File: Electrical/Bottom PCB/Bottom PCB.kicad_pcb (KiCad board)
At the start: 2 copper layers, 100 x 80 mm, 61 parts, among them J101 Steper1, J102 Steper2, J104 Servo1, J105 Servo2, J106 Servo3, J107 Servo4, J201 PROGRAMMING, J202 MainIO, Q201 BC847, Q202 BC847, SW101 FL, SW102 FR, U101 ULN2003A, U103 QRE1113, U106 QRE1113, U107 MCP23017_SO, U108 QRE1113, U109 QRE1113, U201 ESP32-WROVER

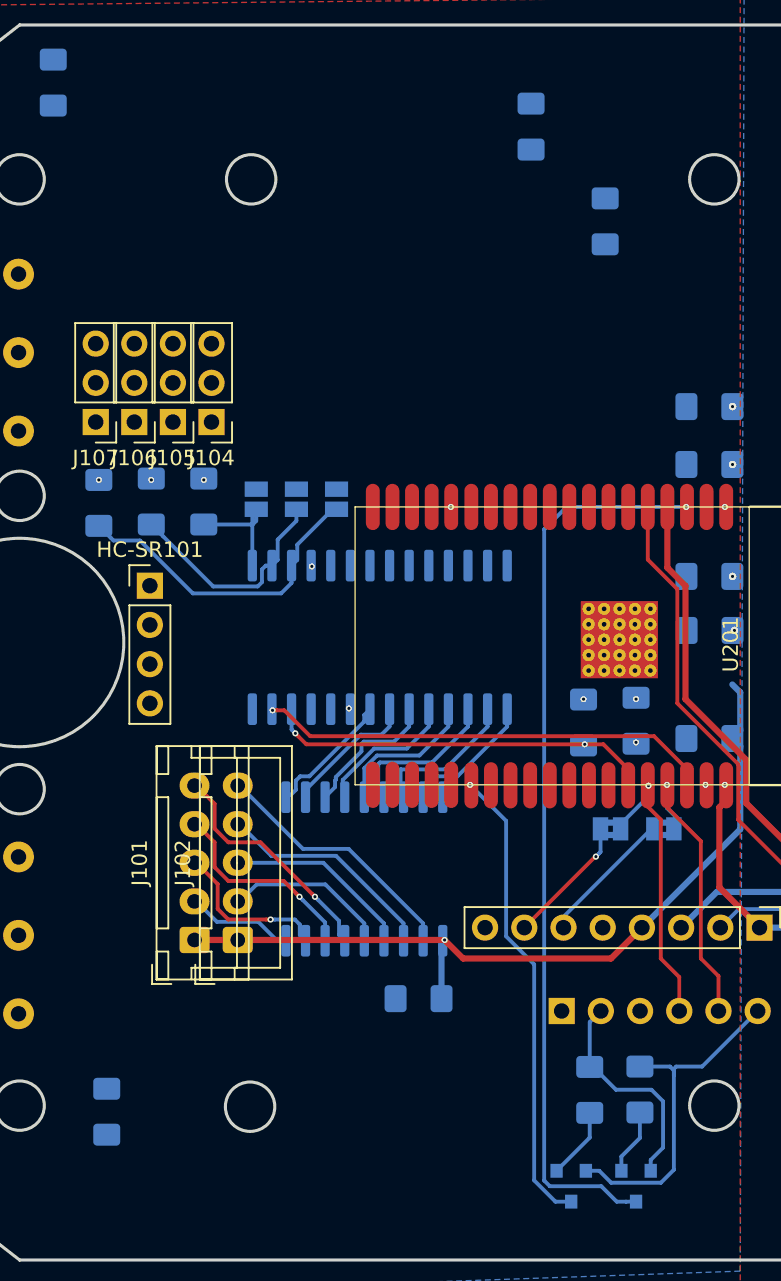
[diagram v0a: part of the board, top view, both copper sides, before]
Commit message: moved some parts to 5V supply
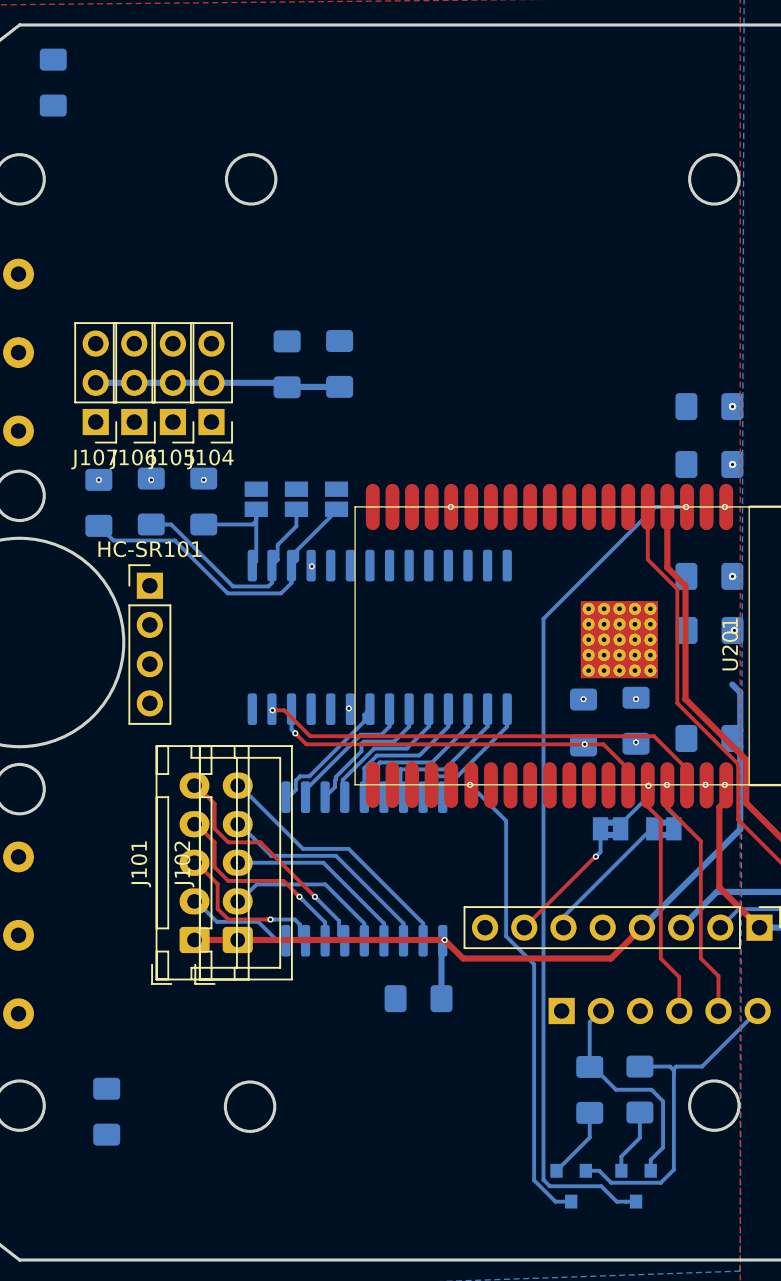
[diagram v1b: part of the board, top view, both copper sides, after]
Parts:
- moved C103 22.1 mm to (136.4, 71.5)
- moved C102 19.5 mm to (139.8, 71.5)
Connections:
- J104 pad 2: Net-(J104-Pad2) -> +5V
- J105 pad 2: Net-(J104-Pad2) -> +5V
- J106 pad 2: Net-(J104-Pad2) -> +5V
- J107 pad 2: Net-(J104-Pad2) -> +5V
- R104 pad 2: +5V -> +3V3
- R106 pad 2: +5V -> +3V3
- R108 pad 2: +5V -> +3V3
- R113 pad 2: +5V -> +3V3
- SW101 pad 1: +5V -> +3V3
- SW102 pad 1: +5V -> +3V3
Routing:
- net +5V: track 53.1 -> 69.0 mm
- net EN: track 58.5 -> 55.2 mm

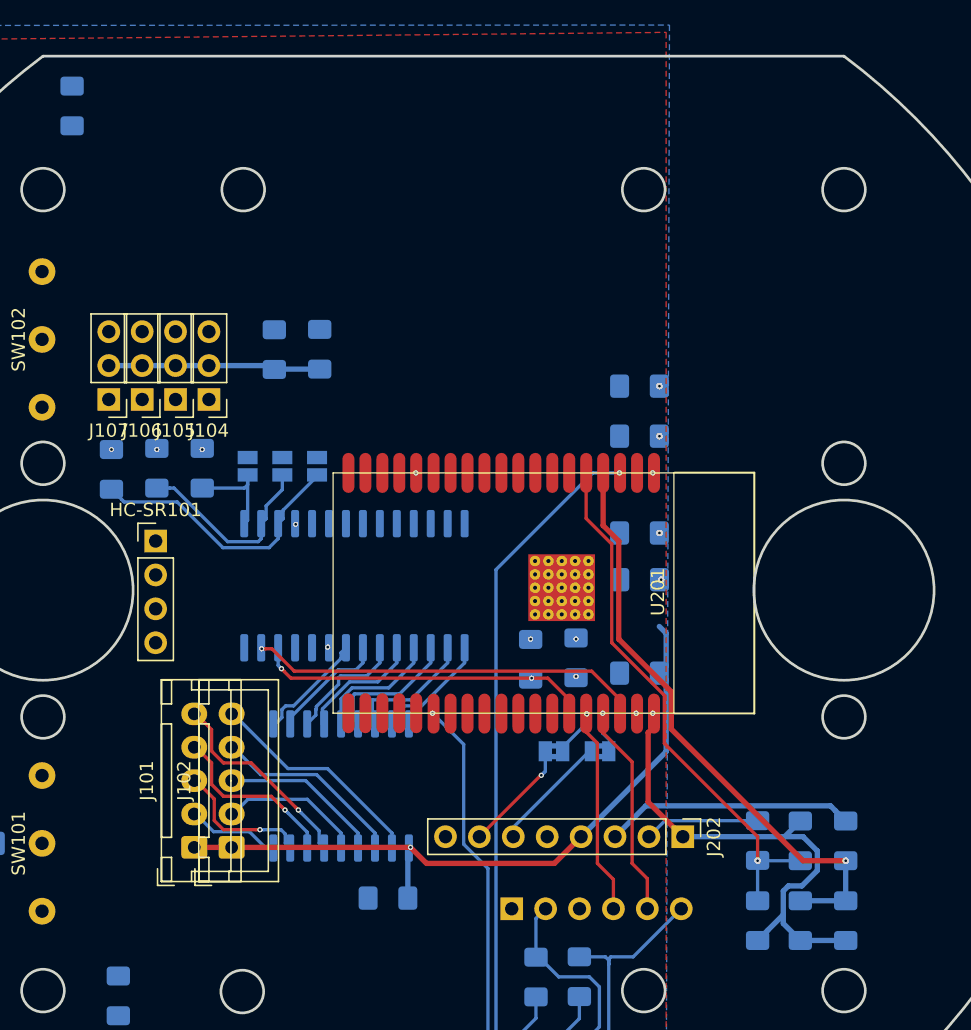
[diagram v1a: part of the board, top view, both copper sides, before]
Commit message: removed the servos at the moment
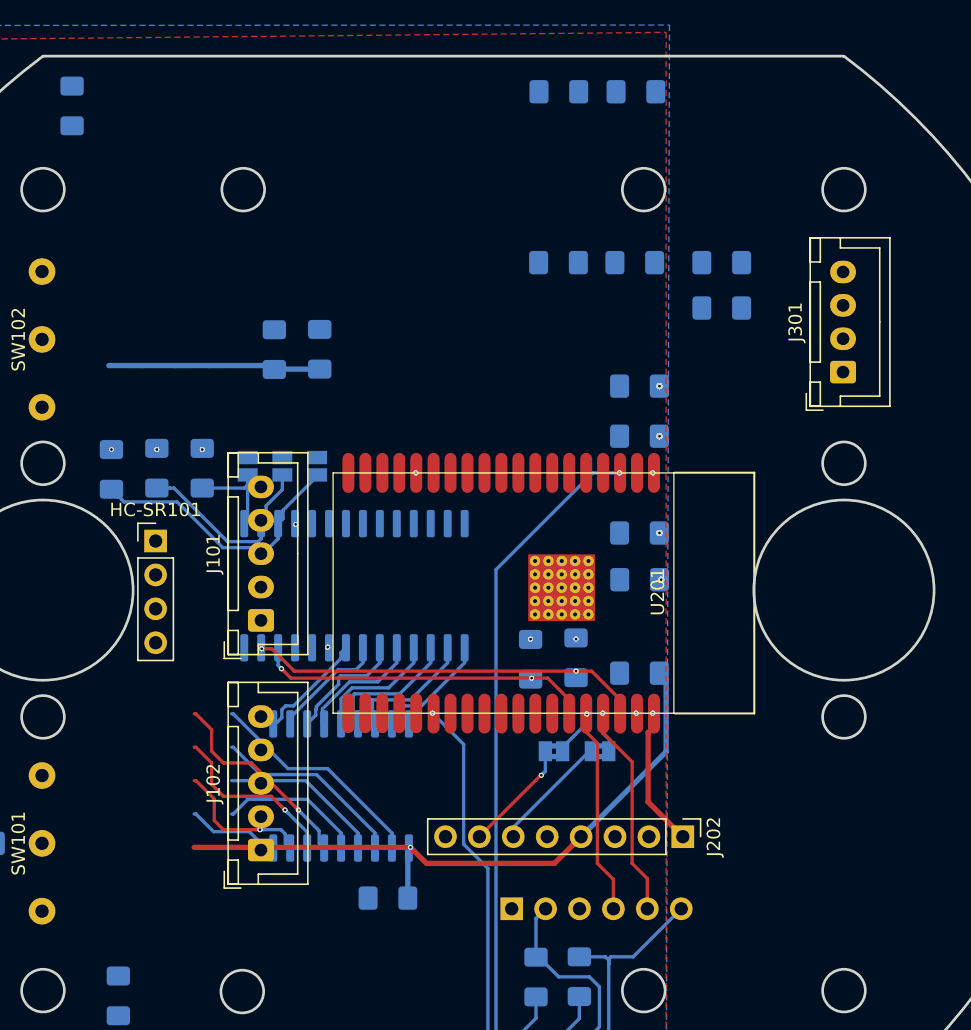
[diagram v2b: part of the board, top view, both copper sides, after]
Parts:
- removed J104: Servo1, Connector_PinHeader_2.54mm:PinHeader_1x03_P2.54mm_Vertical
- removed J105: Servo2, Connector_PinHeader_2.54mm:PinHeader_1x03_P2.54mm_Vertical
- removed J106: Servo3, Connector_PinHeader_2.54mm:PinHeader_1x03_P2.54mm_Vertical
- removed J107: Servo4, Connector_PinHeader_2.54mm:PinHeader_1x03_P2.54mm_Vertical
- added J301: Battery, Connector_JST:JST_XH_B4B-XH-A_1x04_P2.50mm_Vertical, F.Cu at (179.0, 73.2)
- moved C301 64.7 mm to (157.7, 52.2), turned to 0 degrees
- moved R304 62.8 mm to (163.5, 52.2), turned to 0 degrees
- moved R302 53.8 mm to (157.7, 65.0), turned to 180 degrees
- moved C302 45.1 mm to (163.4, 65.0), turned to 180 degrees
- moved R303 43.4 mm to (169.9, 65.0), turned to 0 degrees
- moved R301 41.0 mm to (169.9, 68.4), turned to 0 degrees
- moved J101 17.7 mm to (135.4, 91.8)
- moved J102 2.21 mm to (135.4, 109.0)
- renumbered C107 to C103, C103 to C104, C104 to C105, C109 to C106, C110 to C107, C111 to C108, R109 to R105, R110 to R106, R111 to R107, R105 to R108, R106 to R109, R107 to R110, R108 to R111, U103 to U102, U107 to U103, U106 to U104, U108 to U105, U109 to U106
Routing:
- net BatV: track 44.9 -> 0.00 mm, vias 1 -> 0
- net half_BatV: track 40.6 -> 0.00 mm, vias 1 -> 0
- net GND: track 37.7 -> 10.5 mm
- net +BATT: track 18.7 -> 0.00 mm
- net +3V8: track 8.64 -> 0.00 mm
- net +5V: track 69.0 -> 65.1 mm

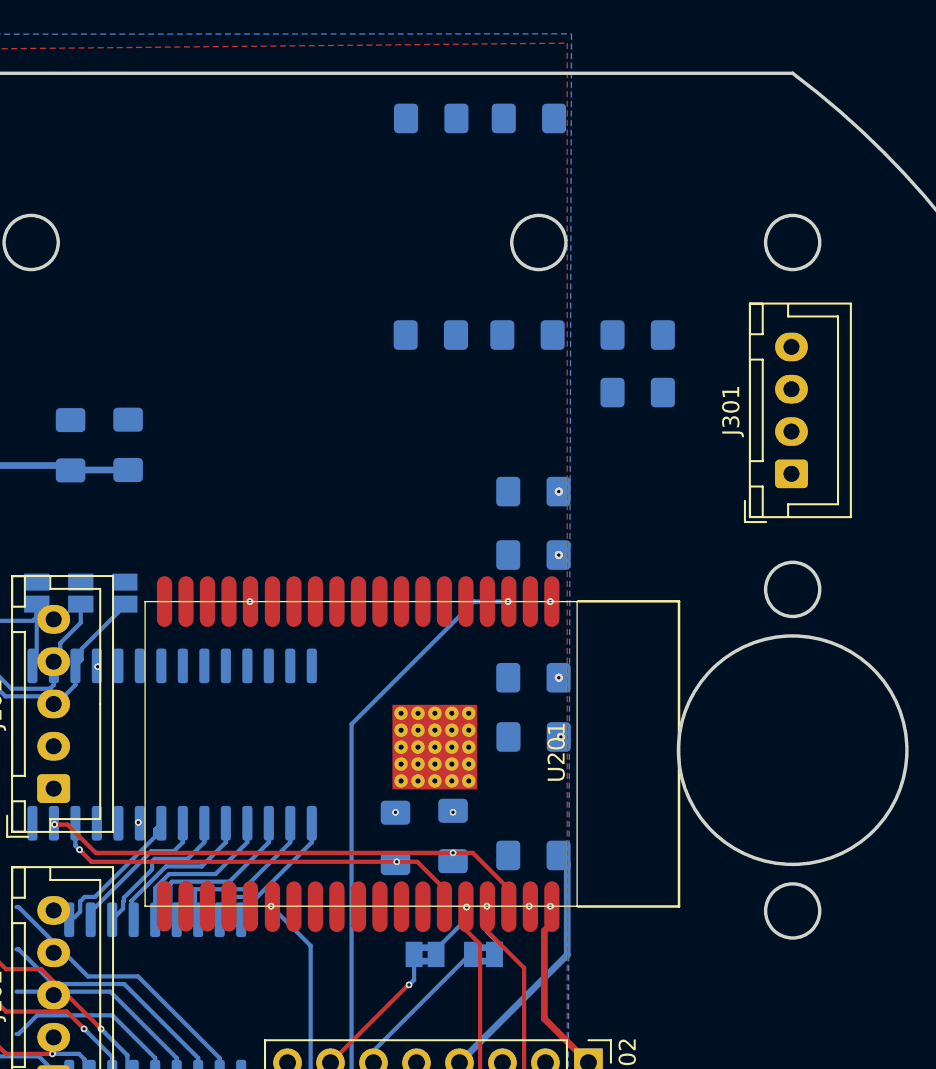
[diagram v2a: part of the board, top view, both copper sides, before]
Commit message: Added power switch
Some more modifications
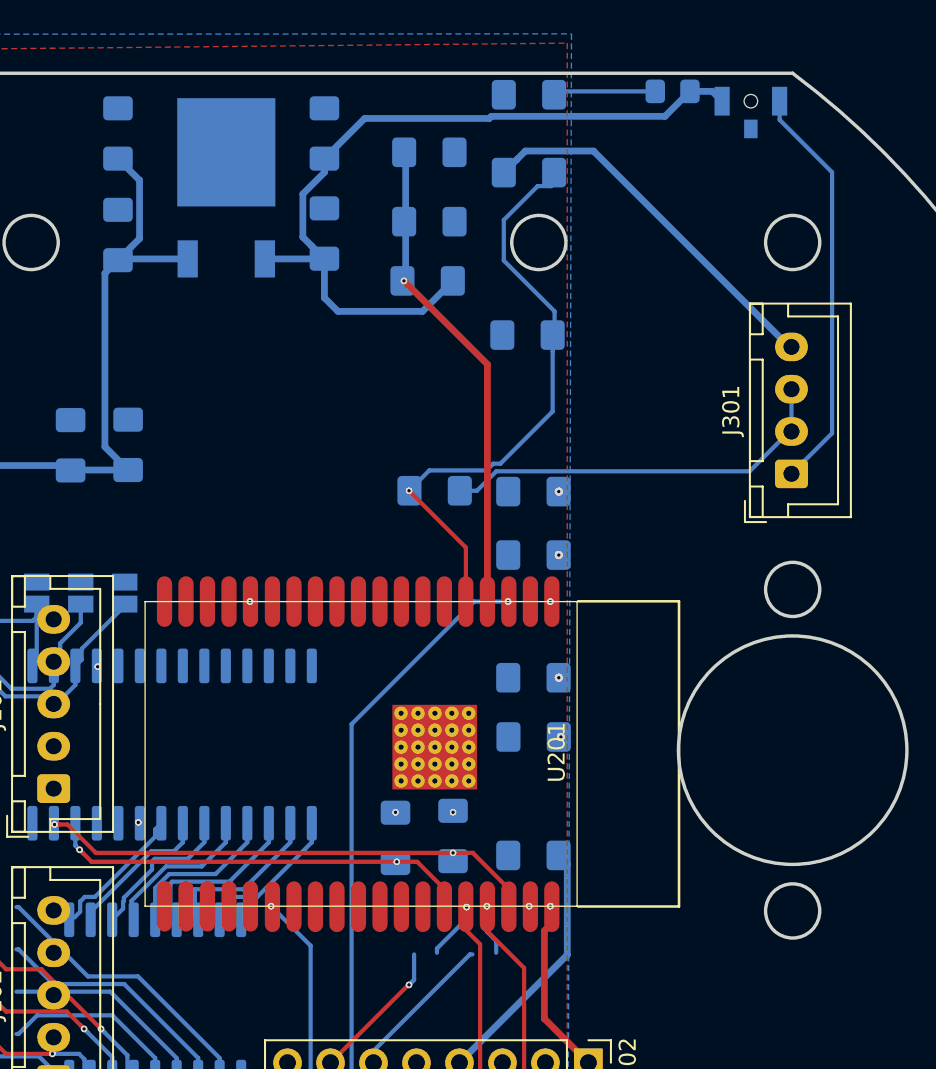
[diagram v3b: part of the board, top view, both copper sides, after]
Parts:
- removed JP201, JP202: Jumper_2_Bridged, Jumper:SolderJumper-2_P1.3mm_Bridged2Bar_Pad1.0x1.5mm
- added C302: 100pF, Capacitor_SMD:C_1206_3216Metric_Pad1.42x1.75mm_HandSolder, B.Cu at (151.4, 59.0)
- added C303: 10uF, Capacitor_SMD:C_1206_3216Metric_Pad1.42x1.75mm_HandSolder, B.Cu at (151.4, 53.1)
- added C304: 10uF, Capacitor_SMD:C_1206_3216Metric_Pad1.42x1.75mm_HandSolder, B.Cu at (139.2, 59.1)
- added C305: 100pF, Capacitor_SMD:C_1206_3216Metric_Pad1.42x1.75mm_HandSolder, B.Cu at (139.2, 53.1)
- added D301: Power, LED_SMD:LED_0805_2012Metric_Pad1.15x1.40mm_HandSolder, B.Cu at (172.0, 50.6)
- added R305: 470, Resistor_SMD:R_1206_3216Metric_Pad1.42x1.75mm_HandSolder, B.Cu at (163.5, 50.8)
- added SW301: SW_SPST, Button_Switch_SMD:SW_SPST_B3U-3100P-B, B.Cu at (176.6, 52.0)
- added U301: MC78M05_TO252, Package_TO_SOT_SMD:TO-252-2, B.Cu at (145.6, 56.3)
- R107: renamed from R105; value 4k7 -> 47k
- R108: renamed from R106; value 4k7 -> 47k
- R109: renamed from R107; value 4k7 -> 47k
- R301, R303: value 22k -> 47k
- moved R303 15.1 mm to (157.9, 74.2)
- moved R301 14.1 mm to (157.5, 61.8)
- moved R302 6.70 mm to (157.6, 58.3)
- moved R304 3.20 mm to (163.5, 55.4)
- moved C301 2.00 mm to (157.6, 54.2)
- renumbered C103 to C101, C101 to C102, C102 to C103, C302 to C306, R108 to R105, R109 to R106, U102 to U101, U101 to U102
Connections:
- J202 pad 2: +3V8 -> (no net)
- J202 pad 3: +BATT -> (no net)
- J202 pad 6: /ESP32-WROVER/TX_sw -> TX
- J202 pad 7: /ESP32-WROVER/RX_sw -> RX
- J301 pad 1: +BATT -> Net-(J301-Pad1)
- J301 pad 2: +3V8 -> half_Bat
- J301 pad 3: +3V8 -> half_Bat
- R303 pad 2: +3V8 -> half_Bat
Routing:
- net +BATT: track 0.00 -> 46.9 mm
- net half_BatV: track 0.00 -> 35.2 mm, vias 0 -> 1
- net BatV: track 0.00 -> 28.6 mm, vias 0 -> 1
- net +5V: track 65.1 -> 89.6 mm
- net Net-(J301-Pad1): track 0.00 -> 24.3 mm
- net half_Bat: track 0.00 -> 23.5 mm
- net GND: track 10.5 -> 32.8 mm
- net TX: track 19.0 -> 27.9 mm
- net /ESP32-WROVER/TX_sw: track 8.91 -> 0.00 mm
- net RX: track 18.9 -> 27.4 mm, vias 1 -> 2
- net /ESP32-WROVER/RX_sw: track 8.47 -> 0.00 mm, vias 1 -> 0
- net Net-(U102-Pad1): track 8.46 -> 0.00 mm
- net Net-(U101-Pad1): track 0.00 -> 8.46 mm
- net Net-(D301-Pad1): track 0.00 -> 6.06 mm

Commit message: added more stuff
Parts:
- added R102: 2k7, Resistor_SMD:R_1206_3216Metric_Pad1.42x1.75mm_HandSolder, B.Cu at (144.5, 106.3)
- added R103: 4k7, Resistor_SMD:R_1206_3216Metric_Pad1.42x1.75mm_HandSolder, B.Cu at (144.5, 103.0)
- moved J201 30.7 mm to (183.0, 102.7), turned to 180 degrees
- moved J101 26.3 mm to (131.8, 65.7), turned to 270 degrees
- moved U102 13.6 mm to (135.8, 91.8), turned to 180 degrees
- moved J202 12.4 mm to (174.9, 98.4), turned to 0 degrees
- moved R201 9.04 mm to (163.9, 102.2)
- moved R202 8.40 mm to (159.2, 102.3)
- moved J102 6.41 mm to (131.8, 103.7), turned to 270 degrees
- moved U103 6.23 mm to (148.6, 88.6), turned to 0 degrees
- renumbered C302 to C301, C303 to C302, C304 to C303, C305 to C304, C301 to C305, R102 to R104, R103 to R105, R104 to R106, R105 to R107, R106 to R108, R107 to R109, R108 to R110, R109 to R111, R110 to R112, R111 to R113, R112 to R114, R113 to R115, R303 to R302, R302 to R303
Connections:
- HC-SR101 pad 2: Sonar -> (no net)
- HC-SR101 pad 3: Sonar -> Net-(HC-SR101-Pad3)
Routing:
- net +5V: track 89.6 -> 0.00 mm, vias 1 -> 0
- net EN: track 55.2 -> 0.00 mm, vias 1 -> 0
- net +BATT: track 46.9 -> 0.00 mm
- net half_BatV: track 35.2 -> 0.00 mm, vias 1 -> 0
- net GND: track 32.8 -> 0.00 mm, vias 3 -> 5
- net GPIO0: track 30.3 -> 0.00 mm, vias 1 -> 0
- net SDA: track 29.5 -> 0.00 mm, vias 2 -> 0
- net BatV: track 28.6 -> 0.00 mm, vias 1 -> 0
- net TX: track 27.9 -> 0.00 mm, vias 1 -> 0
- net RX: track 27.4 -> 0.00 mm, vias 2 -> 0
- net SCL: track 25.2 -> 0.00 mm, vias 2 -> 0
- net Net-(J301-Pad1): track 24.3 -> 0.00 mm
- net half_Bat: track 23.5 -> 0.00 mm
- net /ESP32-WROVER/DTR: track 22.5 -> 0.00 mm
- net Net-(JP101-Pad1): track 20.6 -> 0.00 mm
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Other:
- outline, holes or cut-outs redrawn
- board text added: "SwarmBot copyright Philip McGaw 2020"
